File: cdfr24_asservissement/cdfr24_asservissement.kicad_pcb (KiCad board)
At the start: 2 copper layers, 101.6 x 78.6 mm, 90 parts, among them J1 Connecteur batterie, J10 Connecteur Odométrie, J11 Conn_01x03, J12 Connecteur Odométrie, J13 Conn_01x03, J14 Conn_01x02, J15 Conn_01x02, J2 Conn_01x05, J3 Conn_01x03, J4 Conn_01x08_Pin, J5 Conn_ST_STDC14, J6 Conn_01x05, J7 Connecteur Programmation, J8 Conn_01x03, J9 Conn_01x08_Pin, Q1 Q_NMOS_GDS, SW1 SW_DIP_x02, U1 LD1117S33TR_SOT223, U2 TVN 5-2411WI, U3 STM32F401RCTx

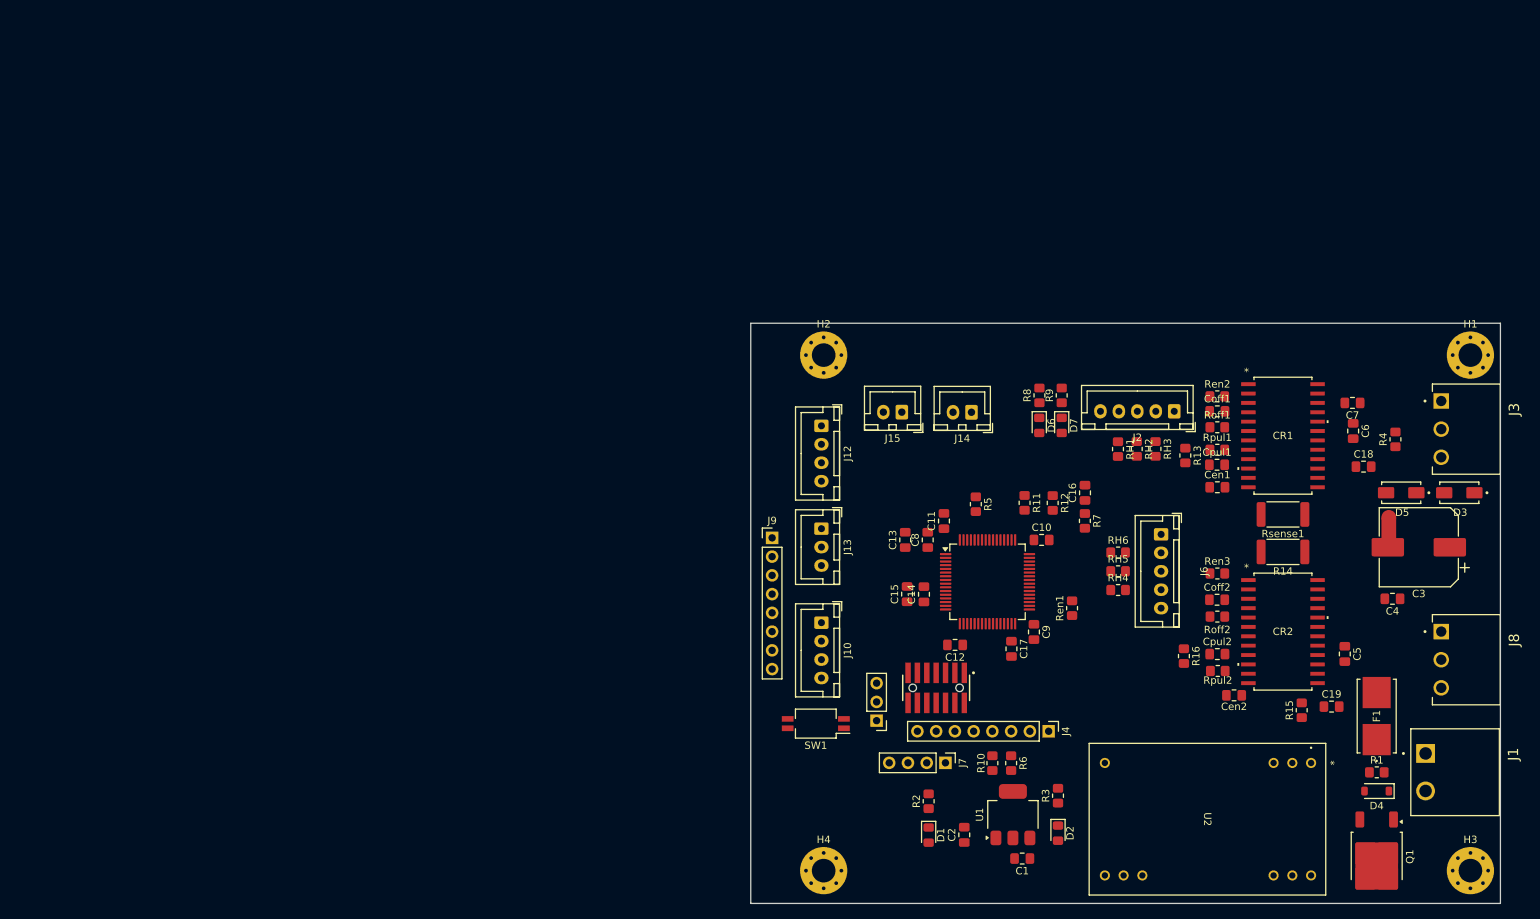
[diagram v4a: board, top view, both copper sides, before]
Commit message: Improve placement
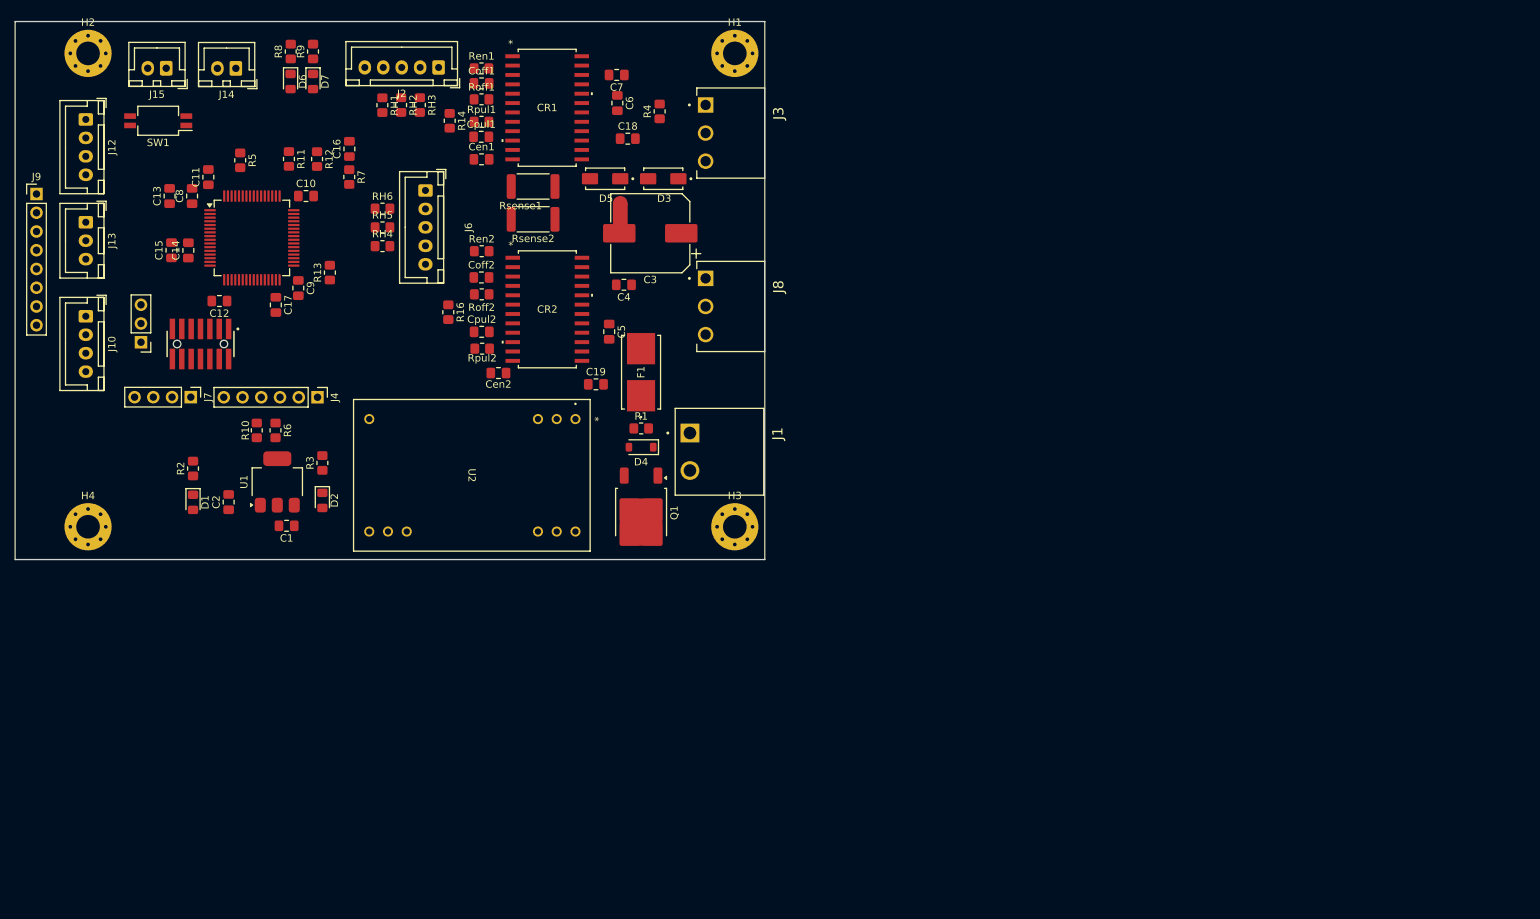
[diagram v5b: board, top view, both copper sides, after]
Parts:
- removed R15: 10k, Resistor_SMD:R_0805_2012Metric_Pad1.20x1.40mm_HandSolder
- removed the Ren1 at (202.6, 106.0)
- added R13: 10k, Resistor_SMD:R_0805_2012Metric_Pad1.20x1.40mm_HandSolder, F.Cu at (102.0, 60.6)
- J4: value Conn_01x08_Pin -> Conn_01x06_Pin; footprint Connector_PinHeader_2.54mm:PinHeader_1x08_P2.54mm_Vertical -> Connector_PinHeader_2.54mm:PinHeader_1x06_P2.54mm_Vertical
- moved SW1 120.9 mm to (78.7, 40.0)
- moved D5 115.9 mm to (139.3, 47.9)
- moved D3 115.9 mm to (147.2, 47.9)
- moved J7 113.6 mm to (83.2, 77.5)
- moved C3 112.5 mm to (145.4, 55.2)
- moved C4 112.5 mm to (141.8, 62.2)
- moved NT1 112.5 mm to (141.4, 53.2)
- moved J11 112.1 mm to (76.4, 70.0)
- moved D6 111.6 mm to (96.7, 34.7)
- moved D7 111.6 mm to (99.7, 34.7)
- moved R8 111.6 mm to (96.7, 30.6)
- moved R9 111.6 mm to (99.7, 30.6)
- moved Rsense2 111.1 mm to (129.5, 53.4)
- moved Rsense1 110.9 mm to (129.5, 48.9)
- moved J8 110.6 mm to (152.9, 61.4)
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- renumbered R13 to R14, Ren2 to Ren1, Ren3 to Ren2, R14 to Rsense2
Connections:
- CR1 pad 14: /BRAKE_L -> /BRAKE_MOT
- CR2 pad 14: /BRAKE_R -> /BRAKE_MOT
- J4 pad 5: unconnected-(J4-Pin_5-Pad5) -> /INT_MAG
- J4 pad 6: unconnected-(J4-Pin_6-Pad6) -> /INT_IMU
- Ren1 pad 1: /EN_L -> /EN_MOT
- Ren2 pad 1: /EN_R -> /EN_MOT
- U3 pad 27: /EN_R -> unconnected-(U3-PB1-Pad27)
- U3 pad 28: /BRAKE_R -> unconnected-(U3-PB2-Pad28)
- U3 pad 35: /EN_L -> /BRAKE_MOT
- U3 pad 36: /BRAKE_L -> /EN_MOT
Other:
- board size 101.6 x 78.6 mm -> 101.6 x 72.9 mm

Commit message: Start routing
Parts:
- removed NT1: NetTie_2, NetTie:NetTie-2_SMD_Pad2.0mm
- added NT2: NetTie_2, NetTie:NetTie-2_SMD_Pad0.5mm, F.Cu at (143.0, 56.4)
- moved C6 3.93 mm to (142.0, 41.4)
- moved F1 3.84 mm to (147.8, 72.9)
- moved C18 2.36 mm to (141.7, 44.7)
- moved C5 2.13 mm to (142.0, 68.6)
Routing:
- net /Vsab: track 0.00 -> 63.3 mm
- net GNDPWR: track 0.00 -> 43.9 mm
- net +BATT: track 0.00 -> 27.0 mm
- net Net-(D3-K): track 0.00 -> 12.5 mm
- net /Vboot: track 0.00 -> 11.9 mm
- net Net-(J1-Pin_2): track 0.00 -> 11.5 mm
- net Net-(CR2B-SENSEA): track 0.00 -> 10.9 mm
- net Net-(CR1B-SENSEA): track 0.00 -> 9.55 mm
- net Net-(C7-Pad1): track 0.00 -> 7.17 mm
- net Net-(D4-K): track 0.00 -> 6.91 mm
- net /Vcp_L: track 0.00 -> 3.70 mm

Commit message: Finish routing
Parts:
- removed J9: Conn_01x08_Pin, Connector_PinHeader_2.54mm:PinHeader_1x08_P2.54mm_Vertical
- added TP1: TestPoint, TestPoint:TestPoint_Keystone_5015_Micro-Minature, F.Cu at (109.0, 42.2)
- added TP2: TestPoint, TestPoint:TestPoint_Keystone_5015_Micro-Minature, F.Cu at (110.2, 72.1)
- added TP3: TestPoint, TestPoint:TestPoint_Keystone_5015_Micro-Minature, F.Cu at (121.9, 48.5)
- added TP4: TestPoint, TestPoint:TestPoint_Keystone_5015_Micro-Minature, F.Cu at (87.6, 85.1)
- added TP5: TestPoint, TestPoint:TestPoint_Keystone_5015_Micro-Minature, F.Cu at (154.9, 76.2)
- added TP6: TestPoint, TestPoint:TestPoint_Keystone_5015_Micro-Minature, F.Cu at (139.1, 95.9)
- added TP7: TestPoint, TestPoint:TestPoint_Keystone_5015_Micro-Minature, F.Cu at (101.0, 96.0)
- added TP8: TestPoint, TestPoint:TestPoint_Keystone_5015_Micro-Minature, F.Cu at (77.5, 95.2)
- moved R14 19.5 mm to (105.9, 55.1)
- moved J2 10.2 mm to (106.7, 31.1), turned to 0 degrees
- moved C18 6.91 mm to (136.1, 48.8), turned to -90 degrees
- moved RH1 5.20 mm to (114.3, 37.5), turned to 90 degrees
- moved RH3 4.99 mm to (109.2, 37.5), turned to 90 degrees
- moved R12 3.82 mm to (96.5, 44.5)
- moved D7 3.20 mm to (96.5, 34.8)
- moved R9 3.20 mm to (96.5, 30.8)
- moved D6 3.14 mm to (99.8, 34.8)
- moved R8 3.14 mm to (99.8, 30.7)
- moved R11 2.70 mm to (99.1, 44.5)
- moved R5 1.52 mm to (88.6, 44.5), turned to 0 degrees
- moved Ren2 1.50 mm to (122.6, 59.2)
- moved D5 1.42 mm to (140.7, 47.8)
- moved NT1 1.02 mm to (143.0, 57.4)
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- renumbered NT2 to NT1, R16 to R15
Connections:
- SW1 pad 1: unconnected-(SW1-Pad1) -> Net-(U3-PB5)
- SW1 pad 2: unconnected-(SW1-Pad2) -> Net-(U3-PB4)
- U3 pad 11: /INT_IMU -> unconnected-(U3-PC3-Pad11)
- U3 pad 2: Free2 -> unconnected-(U3-PC13-Pad2)
- U3 pad 23: unconnected-(U3-PA7-Pad23) -> /INT_IMU
- U3 pad 3: Free3 -> unconnected-(U3-PC14-Pad3)
- U3 pad 4: Free4 -> unconnected-(U3-PC15-Pad4)
- U3 pad 42: /FWD_L -> /FWD_R
- U3 pad 43: /FWD_R -> /FWD_L
- U3 pad 56: unconnected-(U3-PB4-Pad56) -> Net-(U3-PB4)
- U3 pad 57: unconnected-(U3-PB5-Pad57) -> Net-(U3-PB5)
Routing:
- net +5V: track 0.00 -> 198.7 mm
- net +3.3V: track 0.00 -> 198.3 mm, vias 0 -> 9
- net /Vref_DAC: track 0.00 -> 78.2 mm, vias 0 -> 7
- net /BRAKE_MOT: track 0.00 -> 77.7 mm, vias 0 -> 3
- net GNDPWR: track 43.9 -> 119.3 mm, vias 0 -> 8
- net /EN_MOT: track 0.00 -> 57.7 mm, vias 0 -> 2
- net GND: track 0.00 -> 56.9 mm, vias 0 -> 35
- net /FWD_R: track 0.00 -> 43.1 mm, vias 0 -> 2
- net /TACHO_L: track 0.00 -> 41.0 mm, vias 0 -> 2
- net SWDIO: track 0.00 -> 39.2 mm, vias 0 -> 3
- net /FWD_L: track 0.00 -> 38.1 mm
- net /TACHO_R: track 0.00 -> 36.9 mm
- net /left_driver/H3: track 0.00 -> 35.5 mm
- net /right_driver/OUT1: track 0.00 -> 35.1 mm, vias 0 -> 1
- net SWCLK: track 0.00 -> 34.6 mm, vias 0 -> 2
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- added copper zone on B.Cu, net GND
- added copper zone on F.Cu, net GND
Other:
- board size 101.6 x 72.9 mm -> 96.2 x 72.9 mm

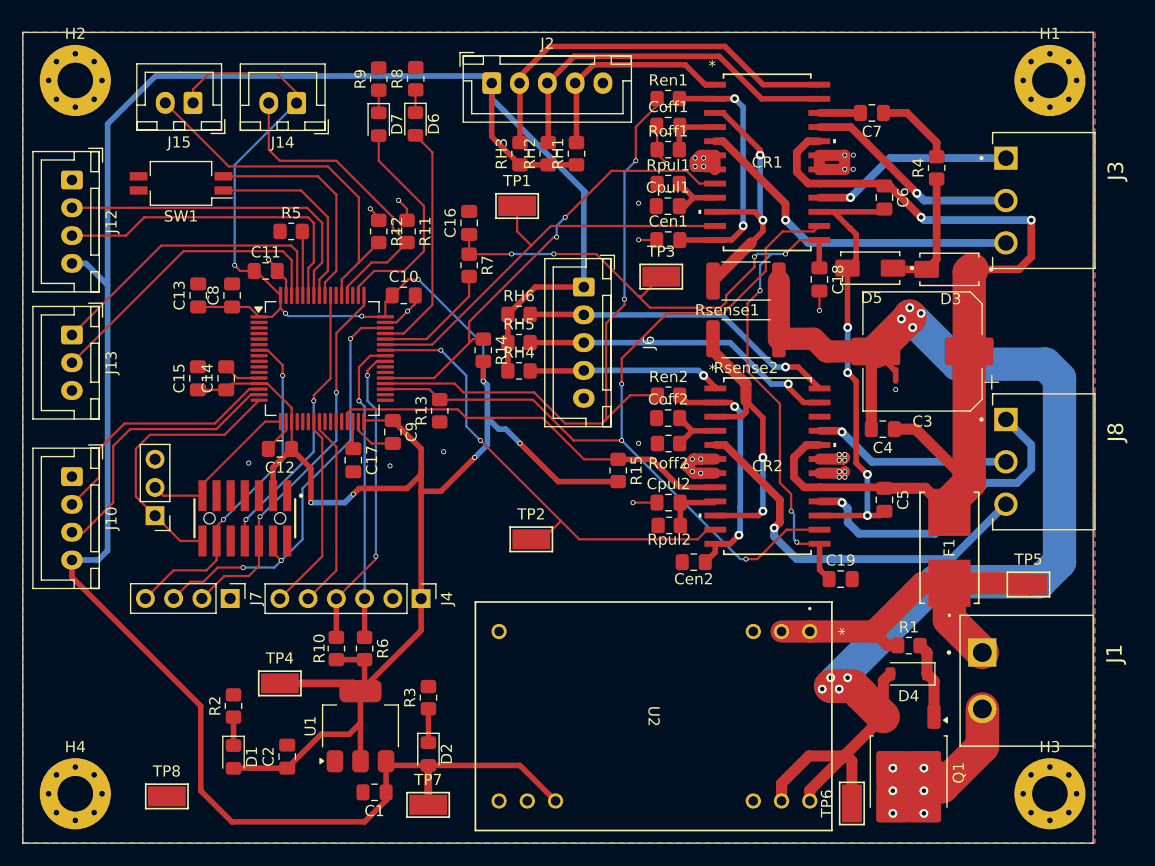
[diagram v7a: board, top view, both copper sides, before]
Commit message: Add silkscreen and logo
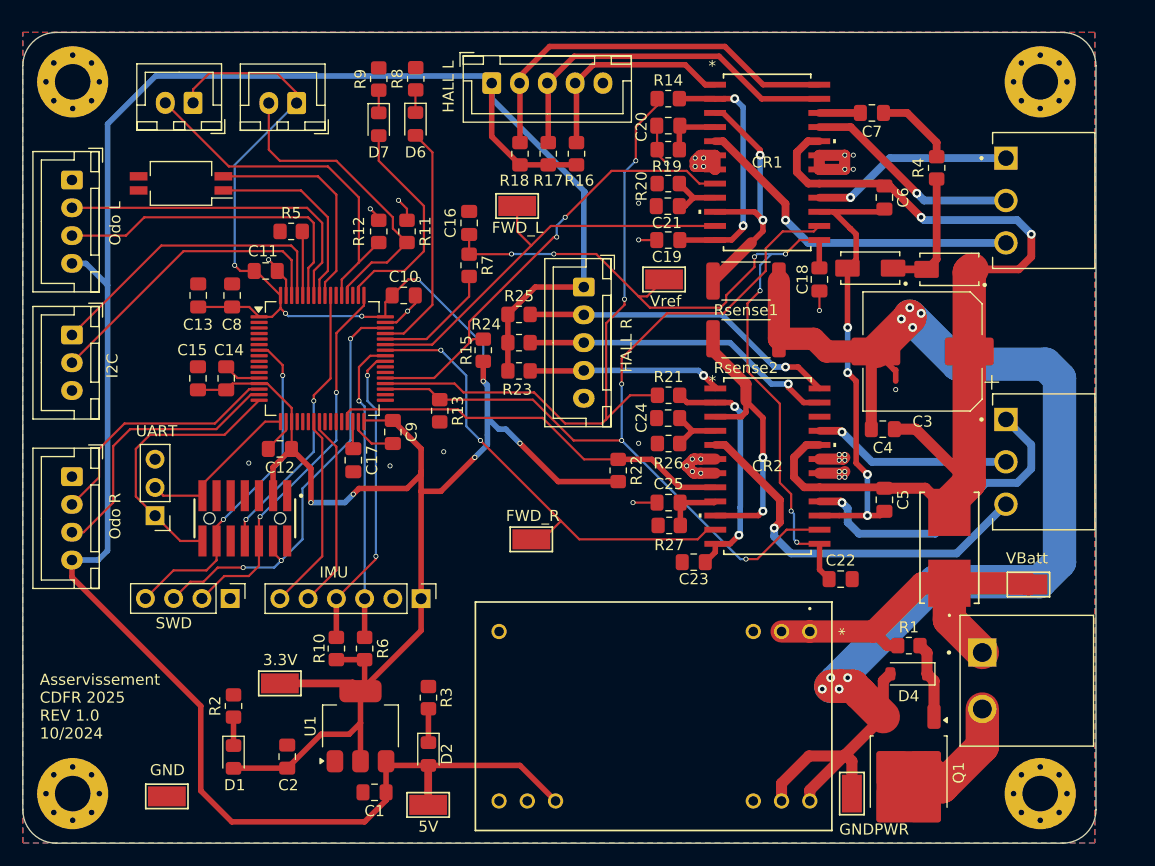
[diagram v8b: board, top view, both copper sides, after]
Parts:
- added G***: LOGO, LOGO:robotronik, B.Cu at (88.9, 47.0)
- moved TP3 0.89 mm to (139.1, 95.0)
- moved H1 0.88 mm to (156.0, 31.0)
- moved H3 0.87 mm to (156.0, 95.0)
- moved TP7 0.36 mm to (122.2, 48.8)
- moved H2 0.27 mm to (69.0, 31.0)
- moved H4 0.24 mm to (69.0, 95.0)
- renumbered Cen1 to C19, Coff1 to C20, Cpul1 to C21, C19 to C22, Cen2 to C23, Coff2 to C24, Cpul2 to C25, J11 to J10, J12 to J11, J13 to J12, J14 to J13, J15 to J14, J10 to J9, Ren1 to R14, R14 to R15, RH1 to R16, RH2 to R17, RH3 to R18, Roff1 to R19, Rpul1 to R20, Ren2 to R21, R15 to R22, RH4 to R23, RH5 to R24, RH6 to R25, Roff2 to R26, Rpul2 to R27, TP4 to TP1, TP5 to TP2, TP6 to TP3, TP7 to TP4, TP8 to TP5, TP1 to TP6, TP3 to TP7, TP2 to TP8
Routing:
- net GNDPWR: track 119.3 -> 118.4 mm
- net /Vsab: track 87.4 -> 86.7 mm
- net Net-(J1-Pin_2): vias 6 -> 0
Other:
- board size 96.2 x 72.9 mm -> 96.5 x 72.9 mm
- board text added: "3.3V"
- board text added: "5V"
- board text added: "Asservissement CDFR 2025 REV 1.0 10/2024"
- board text added: "FWD_L"
- board text added: "FWD_R"
- board text added: "GND"
- board text added: "GNDPWR"
- board text added: "HALL L"
- board text added: "HALL R"
- board text added: "I2C"
- board text added: "IMU"
- board text added: "If in doubt, add more flux - A.M"
- board text added: "Odo L"
- board text added: "Odo R"
- board text added: "SWD"
- board text added: "UART"
- board text added: "VBatt"
- board text added: "Vref"
